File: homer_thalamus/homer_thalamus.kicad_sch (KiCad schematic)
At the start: 20 parts, among them J1 GPIO, J2 MotDrv_Pow_Conn, J3 Right_Motor_Conn, J4 Left_Motor_Conn, J5 Spare_GP_Conn, J6 VBUS_Conn, SW1 SW_PULLDOWN, U1 DRV8874_CARRIER_RIGHT, U2 DRV8874_CARRIER_LEFT, U3 HC-SR04, U4 HiLetGo-GY-521

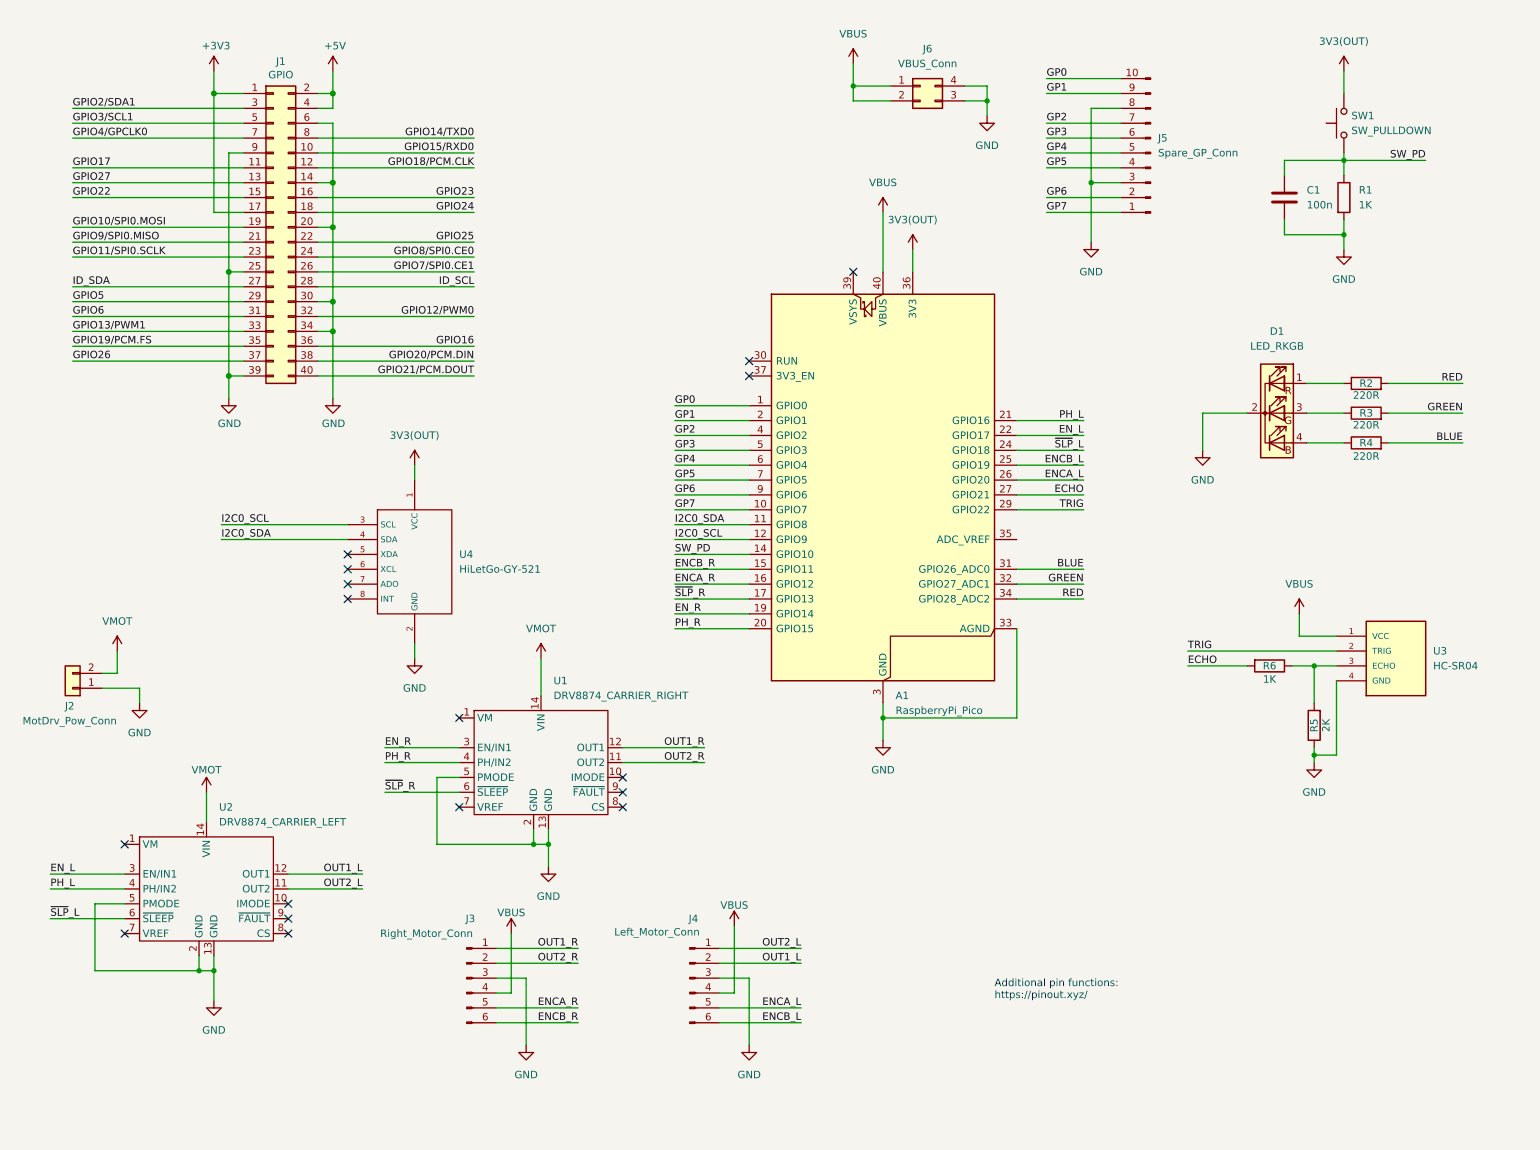
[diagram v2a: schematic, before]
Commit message: start optimize schematic
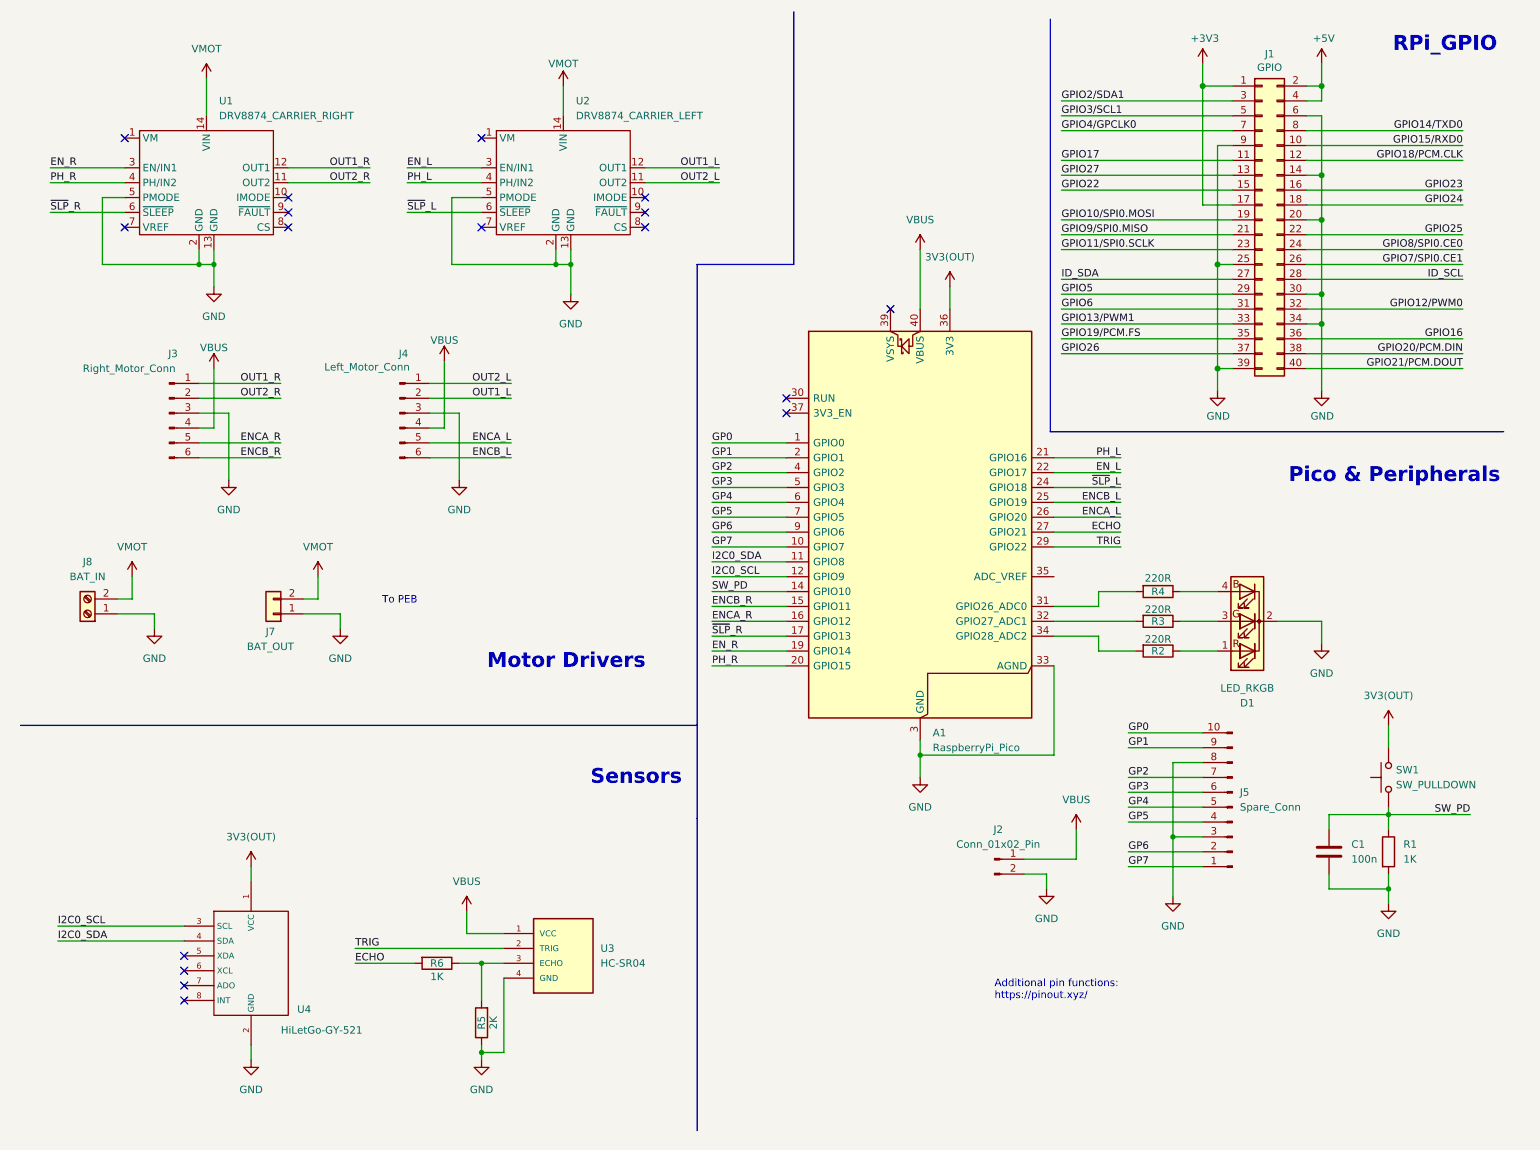
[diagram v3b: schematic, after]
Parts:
- removed J2: MotDrv_Pow_Conn, Connector_JST:JST_XH_B2B-XH-A_1x02_P2.50mm_Vertical, symbol Connector_Generic:Conn_01x02
- removed J6: VBUS_Conn, Connector_PinHeader_2.54mm:PinHeader_2x02_P2.54mm_Vertical, symbol Connector_Generic:Conn_02x02_Counter_Clockwise
- added J2: Conn_01x02_Pin, symbol Connector:Conn_01x02_Pin
- added J7: BAT_OUT, Connector_JST:JST_XH_B2B-XH-A_1x02_P2.50mm_Vertical, symbol Connector_Generic:Conn_01x02
- added J8: BAT_IN, symbol Connector:Screw_Terminal_01x02
- J5: value Spare_GP_Conn -> Spare_Conn
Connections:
- net GND: now also J2.2 (Pin_2), J7.1 (Pin_1), J8.1 (Pin_1)
- net VBUS: now also J2.1 (Pin_1)
- net VMOT: now also J7.2 (Pin_2), J8.2 (Pin_2)
- net BLUE: no longer names the net of A1.31 (GPIO26_ADC0), R4.2
- net GREEN: no longer names the net of A1.32 (GPIO27_ADC1), R3.2
- net RED: no longer names the net of A1.34 (GPIO28_ADC2), R2.2
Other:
- note added: "Motor Drivers"
- note added: "Pico & Peripherals"
- note added: "RPi_GPIO"
- note added: "Sensors"
- note added: "To PEB"
- moved on the sheet: A1, C1, D1, J1, J3, J4, J5, R1, R2, R3, R4, R5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

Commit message: reorganize sch
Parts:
- added J6: PICO_POW, symbol Connector:Conn_01x02_Pin
- J2: value Conn_01x02_Pin -> PICO_5VOUT
- J5: value Spare_Conn -> Spare_GP
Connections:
- net GND: now also J6.2 (Pin_2)
- net VSYS: now reaches A1.39 (VSYS)
- net VSYS: now also J6.1 (Pin_1)
- no-connect marks 17 -> 16
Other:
- moved on the sheet: A1, C1, D1, J2, J3, J4, J5, J7, J8, R1, R2, R3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

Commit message: update footprints
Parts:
- J2: footprint (none) -> Connector_PinHeader_2.54mm:PinHeader_1x02_P2.54mm_Vertical
- J6: footprint (none) -> Connector_PinHeader_2.54mm:PinHeader_1x02_P2.54mm_Horizontal
- J8: footprint (none) -> TerminalBlock:TerminalBlock_MaiXu_MX126-5.0-02P_1x02_P5.00mm
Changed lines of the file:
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@@
 			)
 		)
-		(property "Footprint" ""
+		(property "Footprint" "TerminalBlock:TerminalBlock_MaiXu_MX126-5.0-02P_1x02_P5.00mm"
 			(at 67.31 62.23 0)
 			(effects
@@
 			)
 		)
-		(property "Footprint" ""
+		(property "Footprint" "Connector_PinHeader_2.54mm:PinHeader_1x02_P2.54mm_Horizontal"
 			(at 101.6 121.92 0)
 			(effects
@@
 			)
 		)
-		(property "Footprint" ""
+		(property "Footprint" "Connector_PinHeader_2.54mm:PinHeader_1x02_P2.54mm_Vertical"
 			(at 224.79 101.6 0)
 			(effects

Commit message: reorganize sch
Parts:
- renumbered J8 to J1, J7 to J2, J4 to J3, J3 to J4, J2 to J7, J1 to J8, U2 to U1, U1 to U2
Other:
- moved on the sheet: A1, C1, D1, J1, J2, J3, J4, J5, J6, J7, J8, R1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
